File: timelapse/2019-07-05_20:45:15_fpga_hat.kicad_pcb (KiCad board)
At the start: 4 copper layers, 65 x 56.5 mm, 91 parts, among them J1 2x20, J2 AudioJack3, J3 Conn_02x06_Top_Bottom, J4 Conn_02x06_Top_Bottom, J5 Conn_02x06_Top_Bottom, J6 Conn_01x02, SW1 PTS815, SW2 PTS815, SW3 PTS815, SW4 PTS815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

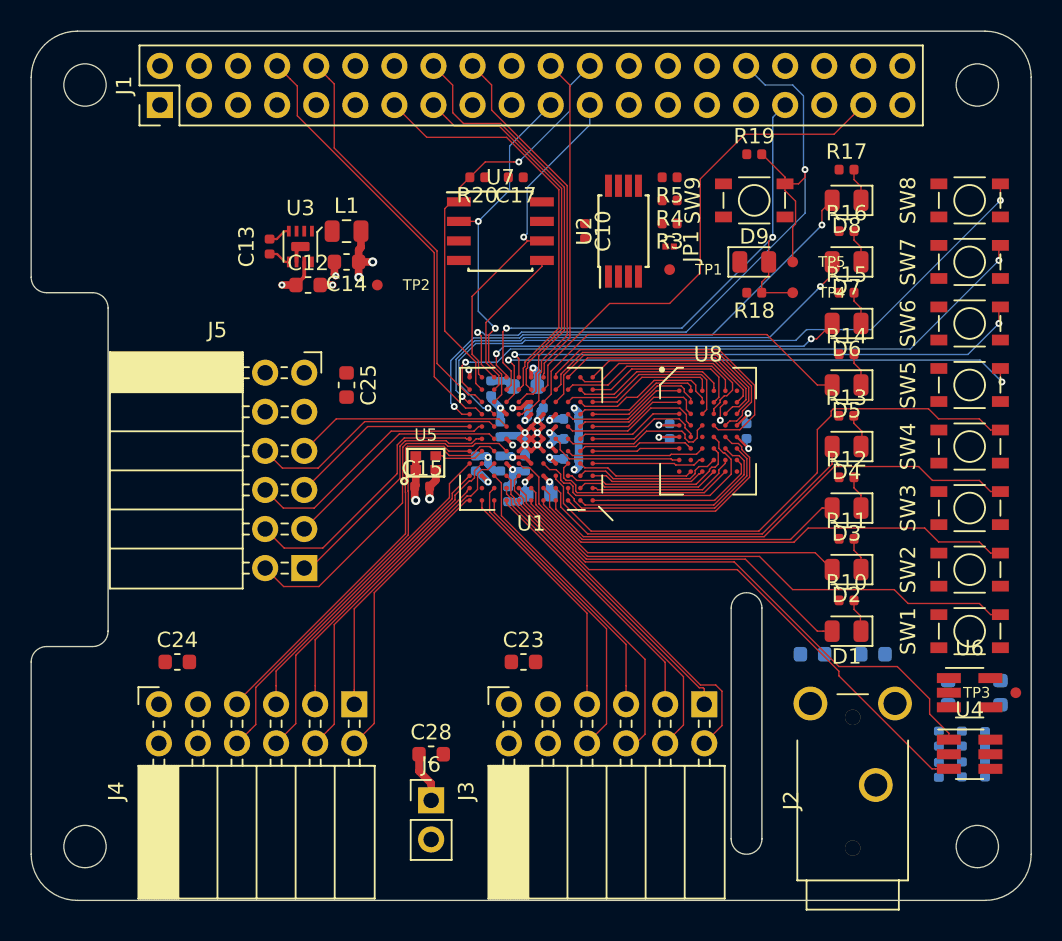
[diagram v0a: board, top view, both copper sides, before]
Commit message: Connect up SDIO, remaining buttons + LEDs.
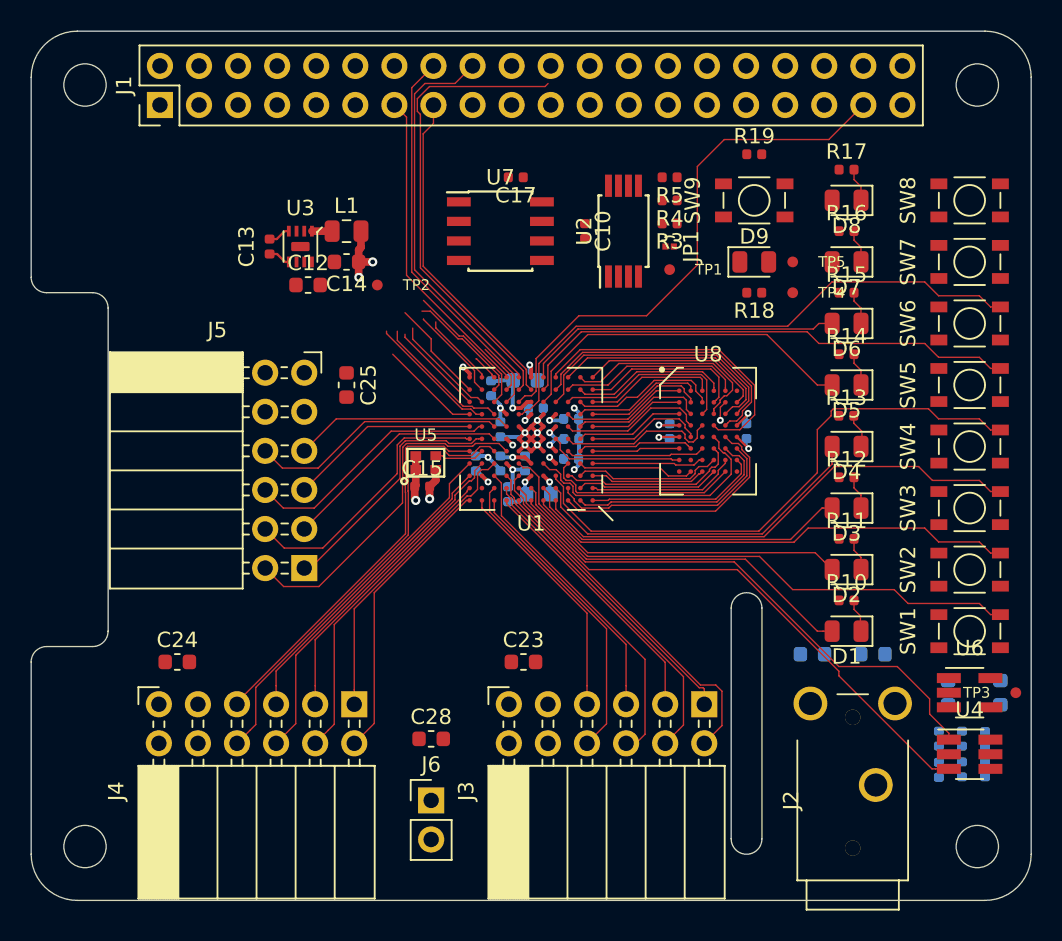
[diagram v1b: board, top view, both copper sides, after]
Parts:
- removed R20: 4k7, Resistor_SMD:R_0402_1005Metric
- moved C28 1.00 mm to (126.0, 126.0)
- moved C2 0.40 mm to (132.1, 102.7)
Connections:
- R5 pad 2: /ID_SD -> /ID_SC
- U1 pad H7: /GP24_SDIO_DAT0 -> /SW5
- U1 pad H9: /SW7 -> /GP25_SDIO_DAT1
- U1 pad J7: /GP23_SDIO_CMD -> /GP26_SDIO_DAT2
- U1 pad J8: /SW4 -> /GP23_SDIO_CMD
- U1 pad K5: /GP26_SDIO_DAT2 -> /SW4
- U1 pad K7: /GP27_SDIO_DAT3 -> /SW7
- U1 pad L5: /GP25_SDIO_DAT1 -> /LED5
- U1 pad L7: /SW5 -> /GP24_SDIO_DAT0
- U1 pad L8: /LED5 -> /GP27_SDIO_DAT3
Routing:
- net /GP12_FPGA_~RST: track 50.2 -> 1.73 mm, vias 2 -> 0
- net /GP13_FPGA_CDONE: track 39.0 -> 3.43 mm, vias 2 -> 0
- net /SW6: track 40.5 -> 6.74 mm, vias 2 -> 0
- net /LED7: track 33.9 -> 6.62 mm, vias 2 -> 0
- net /LED6: track 30.8 -> 6.14 mm, vias 2 -> 0
- net /GP8_SPI_~CS: track 27.5 -> 6.17 mm, vias 1 -> 0
- net /GP14_UART_TXD: track 28.5 -> 8.53 mm
- net /GP15_UART_RXD: track 26.5 -> 6.91 mm
- net /GP11_SPI_SCK: track 22.3 -> 4.84 mm, vias 1 -> 0
- net /GP9_SPI_MISO: track 23.7 -> 9.06 mm, vias 2 -> 0
- net /SW7: track 45.2 -> 30.8 mm, vias 2 -> 0
- net /GP25_SDIO_DAT1: track 21.5 -> 8.89 mm
- net /GP27_SDIO_DAT3: track 27.5 -> 20.7 mm
- net GND: track 33.0 -> 26.9 mm, vias 14 -> 12
- net +5V: track 5.96 -> 0.00 mm, vias 1 -> 0
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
